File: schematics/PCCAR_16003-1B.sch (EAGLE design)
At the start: 24 parts, among them CN1 CARTRIDGE_PCB_52P, U1 UM6650, U2 62256, U3 74F521, U4 74LS05, U5 ICROS16002, U6 ICROS16002, U7 74HC00N

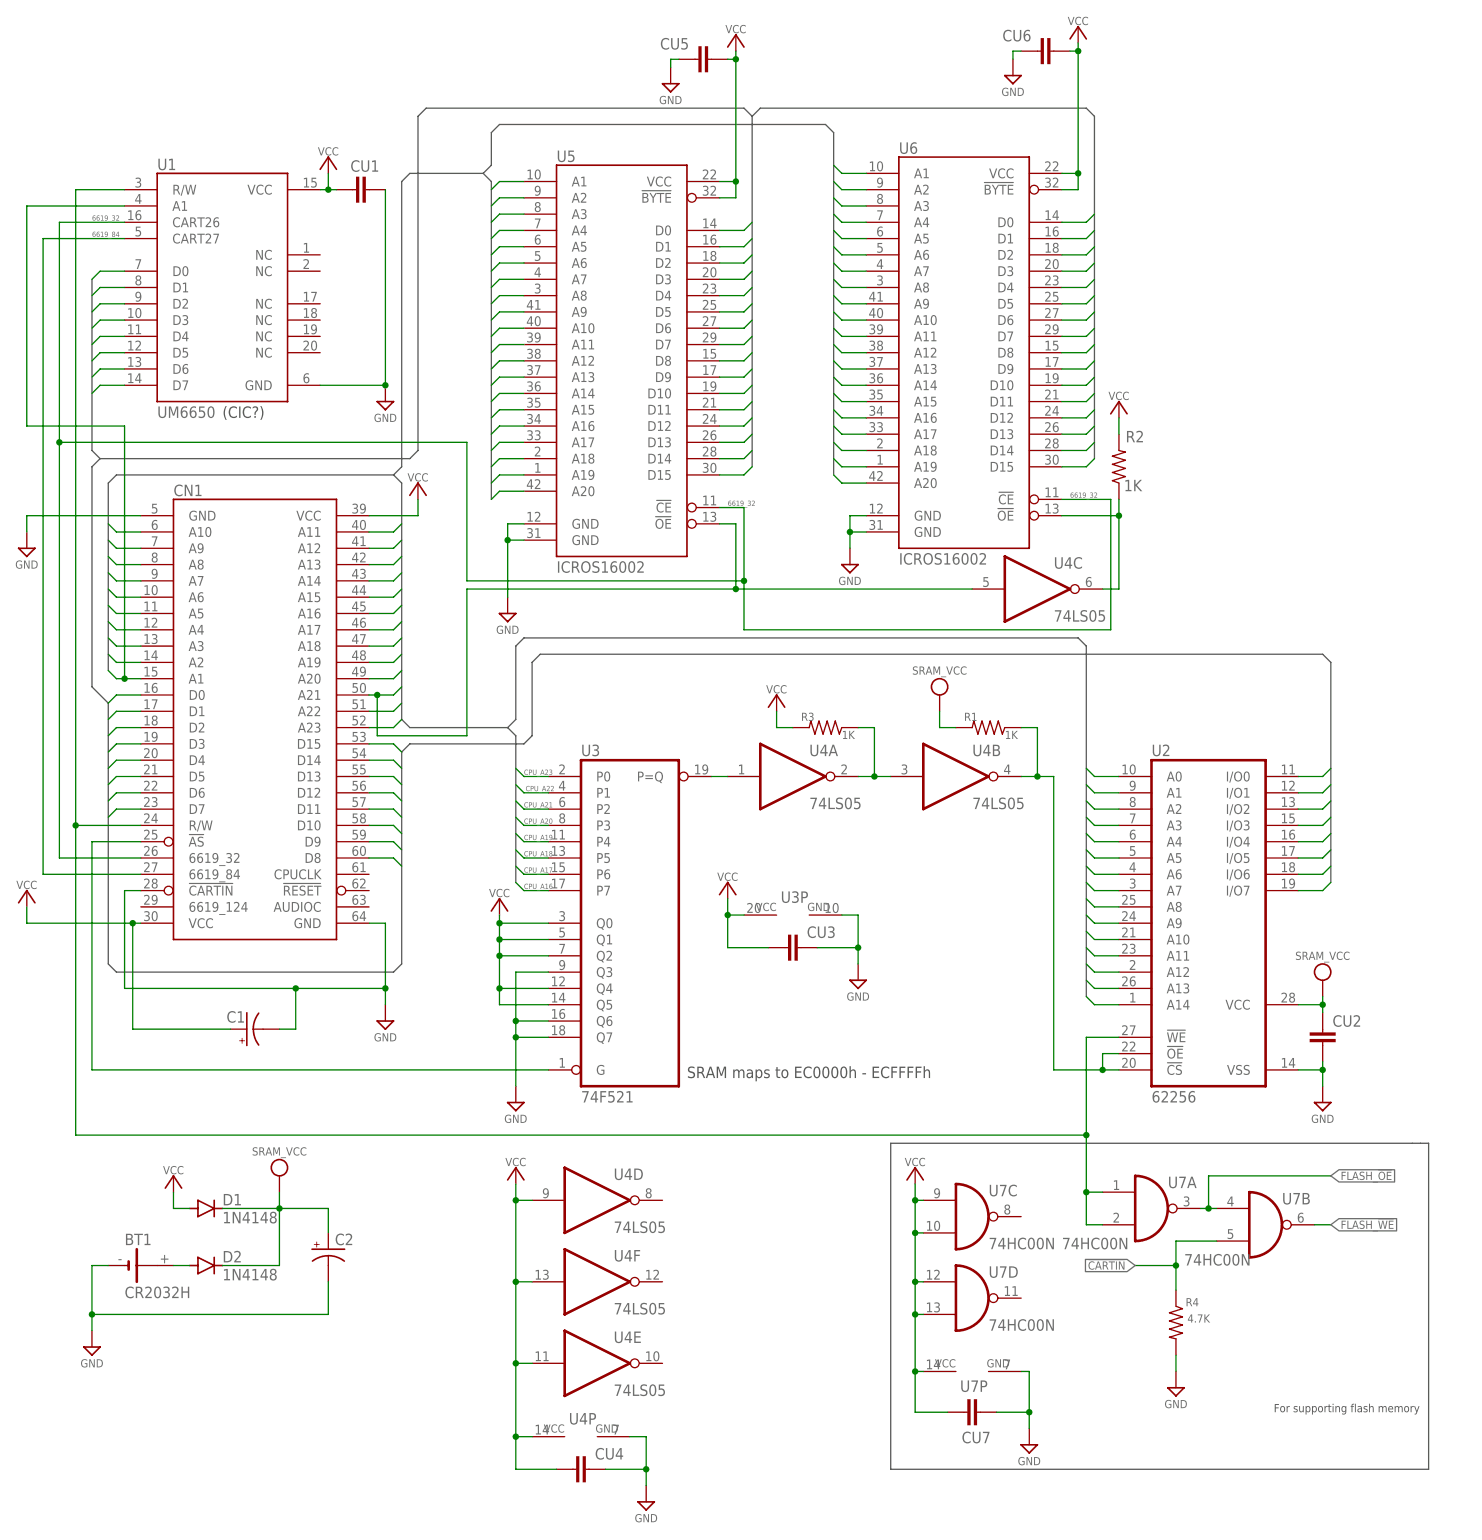
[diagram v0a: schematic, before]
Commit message: Update schematic image files
Removed unused part in cartridge schematic
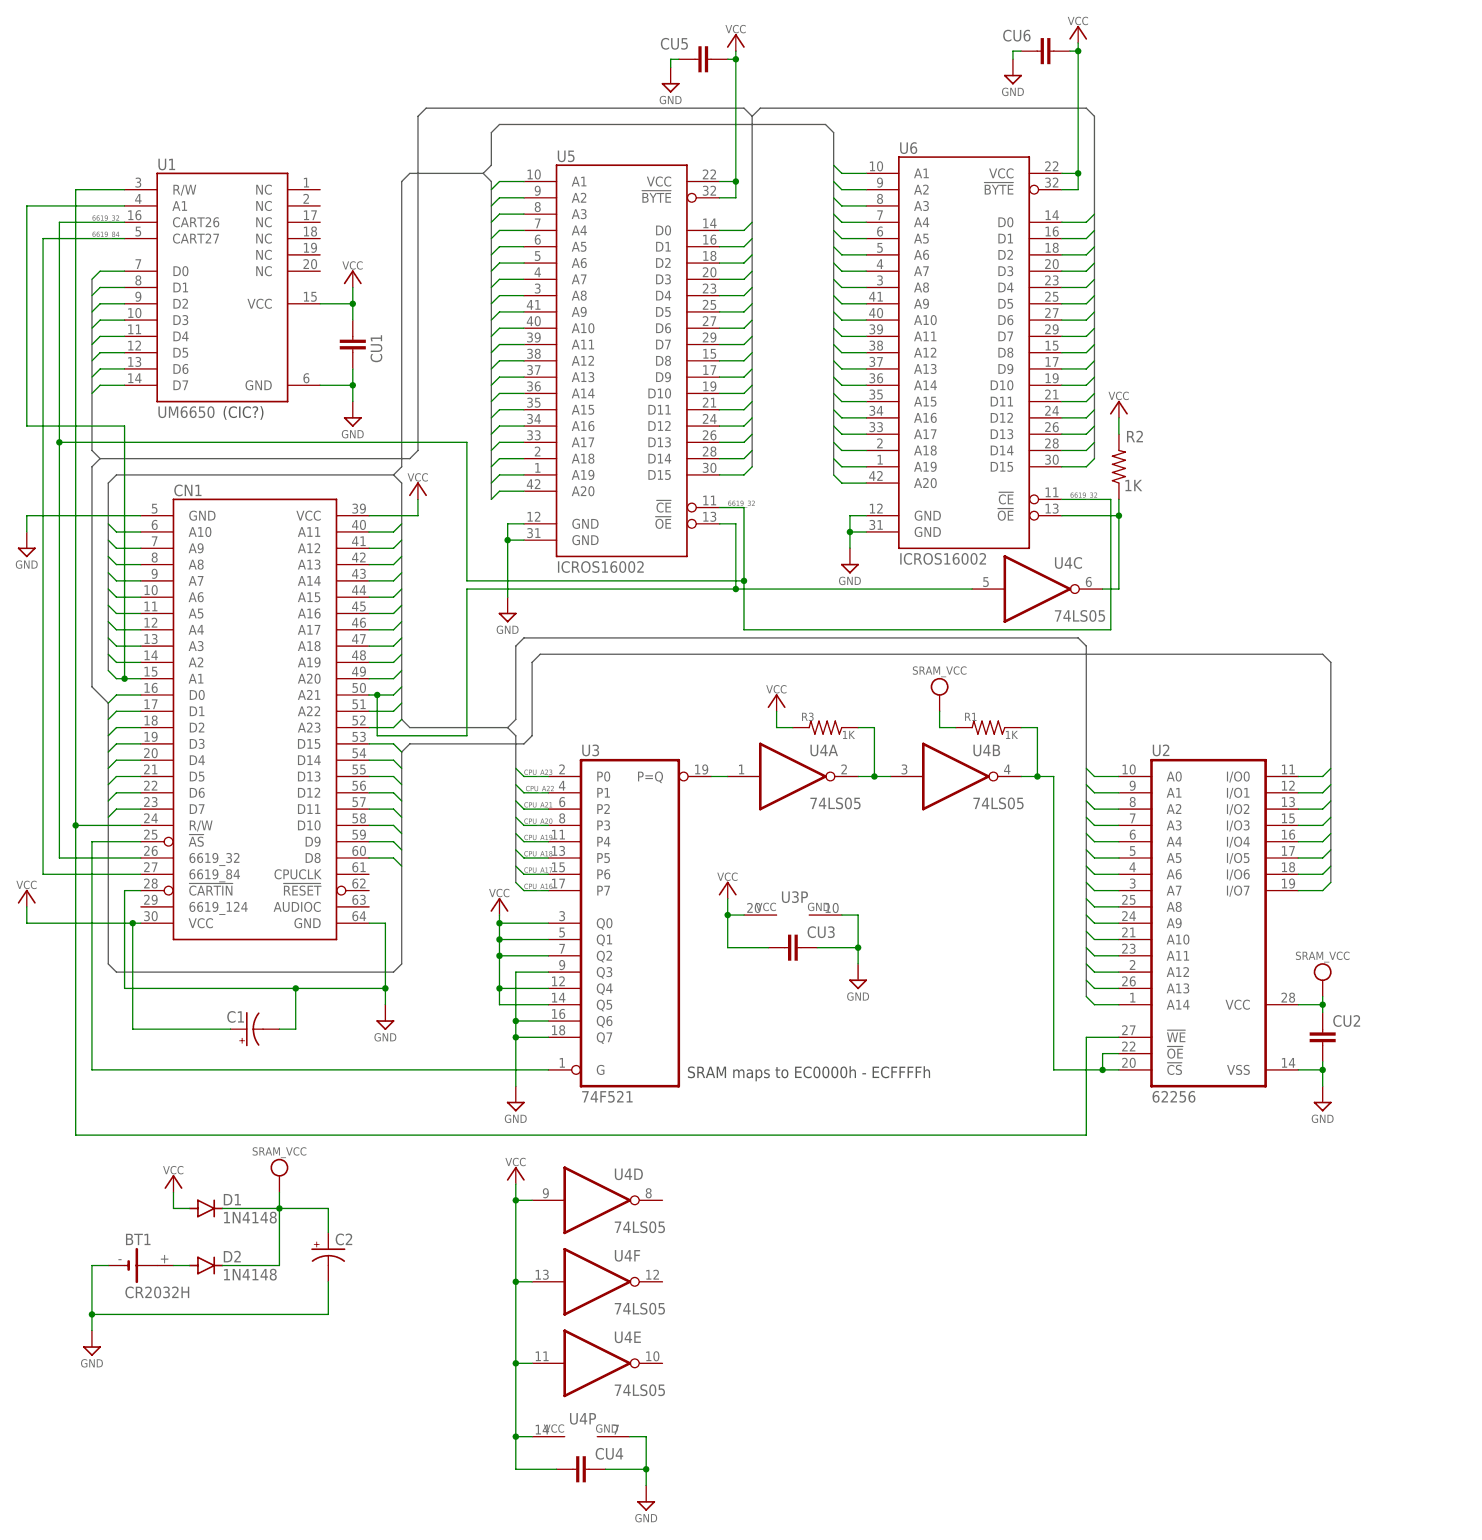
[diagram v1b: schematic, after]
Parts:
- removed CU7: (no value), rcl:C-EUC0805
- removed R4: 4.7K, rcl:R-US_0204/7
- removed U7: 74HC00N, 74xx-eu:74HC00N
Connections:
- removed net !CARTIN: R4.1, U7B.I1
- removed net FLASH_!OE: U7A.O, U7B.I0
- removed net FLASH_!WE: U7B.O
- net GND: no longer CU7.2, R4.2, U7P.GND
- net N$8: no longer U7A.I0, U7A.I1
- net VCC: no longer CU7.1, U7C.I0, U7C.I1, U7D.I0, U7D.I1, U7P.VCC
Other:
- note removed: "For supporting flash memory"
- moved on the sheet: CU1
